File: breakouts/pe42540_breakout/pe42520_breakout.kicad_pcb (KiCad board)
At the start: 4 copper layers, 31.2 x 23.5 mm, 19 parts, among them P101 CONN_01X04, U101 CONN_SMA_2GND, U102 CONN_SMA_2GND, U103 CONN_SMA_2GND, U104 PE42540, U105 CONN_SMA_2GND, U106 CONN_SMA_2GND

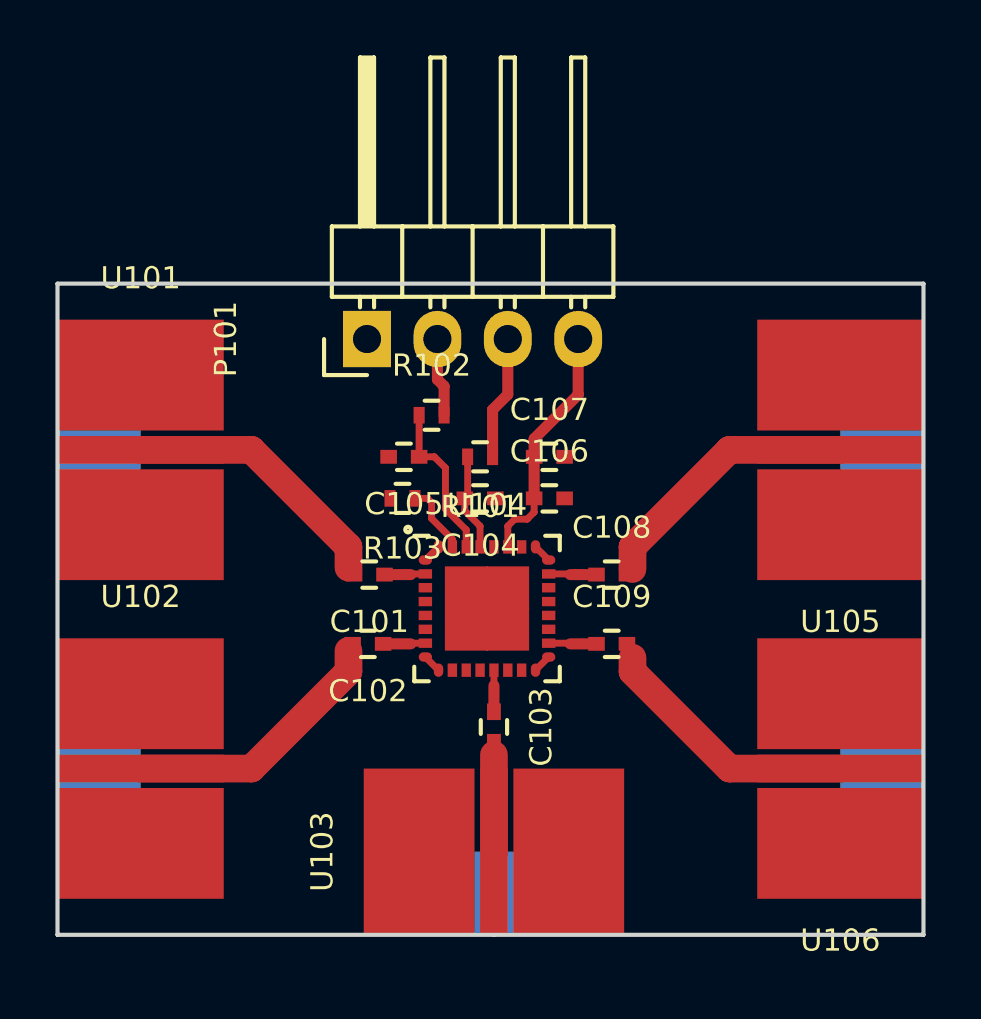
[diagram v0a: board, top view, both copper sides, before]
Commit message: ordered pe42540 breakout
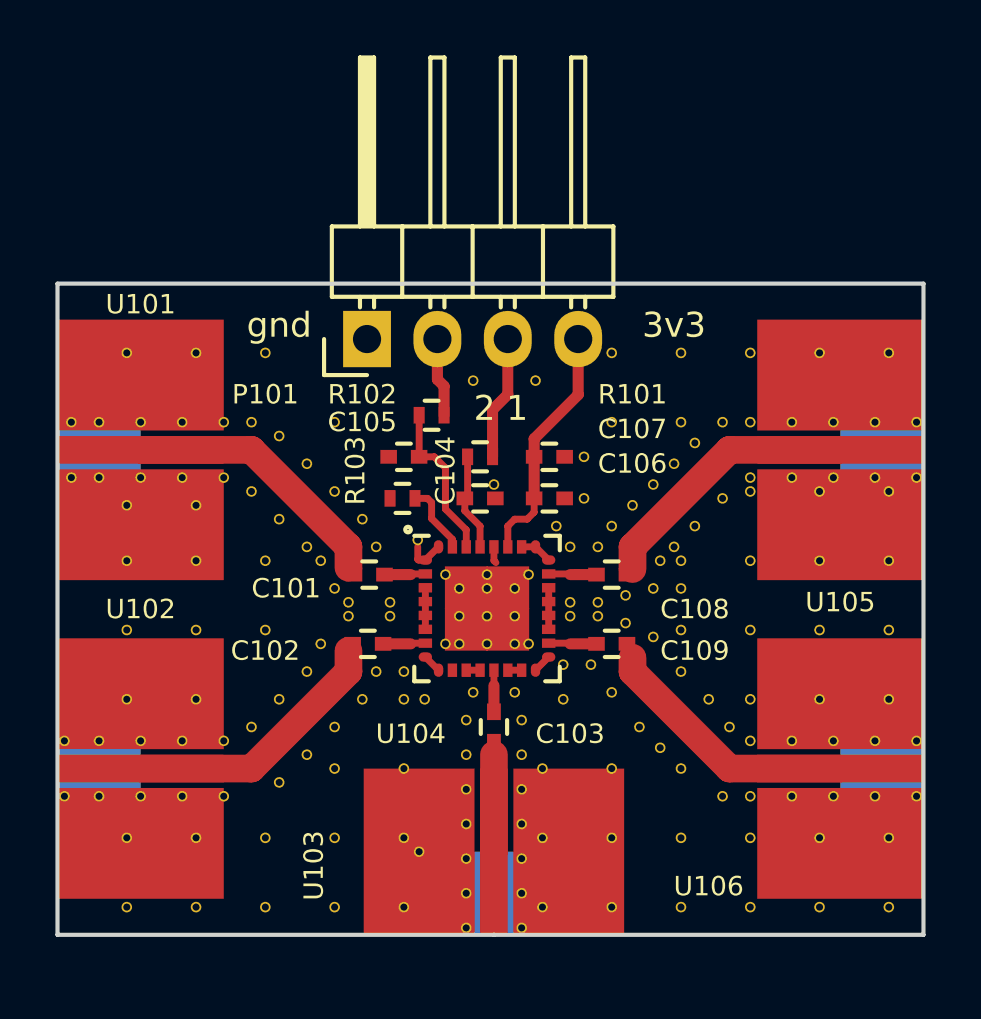
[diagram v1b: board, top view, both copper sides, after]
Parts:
- added REF**: VIA_OSH4LAYER_MIN, vna_footprints:VIA_OSH4LAYER_MIN, F.Cu at (162.5, 86.0)
- added REF**: VIA_OSH4LAYER_MIN, vna_footprints:VIA_OSH4LAYER_MIN, F.Cu at (160.0, 77.5)
- added REF**: VIA_OSH4LAYER_MIN, vna_footprints:VIA_OSH4LAYER_MIN, F.Cu at (154.8, 97.0)
- added REF**: VIA_OSH4LAYER_MIN, vna_footprints:VIA_OSH4LAYER_MIN, F.Cu at (154.8, 98.2)
- added REF**: VIA_OSH4LAYER_MIN, vna_footprints:VIA_OSH4LAYER_MIN, F.Cu at (156.8, 98.2)
- added REF**: VIA_OSH4LAYER_MIN, vna_footprints:VIA_OSH4LAYER_MIN, F.Cu at (152.0, 86.5)
- added REF**: VIA_OSH4LAYER_MIN, vna_footprints:VIA_OSH4LAYER_MIN, F.Cu at (150.5, 86.5)
- added REF**: VIA_OSH4LAYER_MIN, vna_footprints:VIA_OSH4LAYER_MIN, F.Cu at (161.0, 91.0)
- added REF**: VIA_OSH4LAYER_MIN, vna_footprints:VIA_OSH4LAYER_MIN, F.Cu at (162.5, 89.0)
- added REF**: VIA_OSH4LAYER_MIN, vna_footprints:VIA_OSH4LAYER_MIN, F.Cu at (164.0, 80.0)
- added REF**: VIA_OSH4LAYER_MIN, vna_footprints:VIA_OSH4LAYER_MIN, F.Cu at (163.0, 80.8)
- added REF**: VIA_OSH4LAYER_MIN, vna_footprints:VIA_OSH4LAYER_MIN, F.Cu at (161.5, 82.2)
- added REF**: VIA_OSH4LAYER_MIN, vna_footprints:VIA_OSH4LAYER_MIN, F.Cu at (160.0, 80.0)
- added REF**: VIA_OSH4LAYER_MIN, vna_footprints:VIA_OSH4LAYER_MIN, F.Cu at (162.2, 84.5)
- added REF**: VIA_OSH4LAYER_MIN, vna_footprints:VIA_OSH4LAYER_MIN, F.Cu at (160.8, 83.0)
- added REF**: VIA_OSH4LAYER_MIN, vna_footprints:VIA_OSH4LAYER_MIN, F.Cu at (161.5, 86.0)
- added REF**: VIA_OSH4LAYER_MIN, vna_footprints:VIA_OSH4LAYER_MIN, F.Cu at (160.5, 86.2)
- added REF**: VIA_OSH4LAYER_MIN, vna_footprints:VIA_OSH4LAYER_MIN, F.Cu at (158.5, 86.5)
- added REF**: VIA_OSH4LAYER_MIN, vna_footprints:VIA_OSH4LAYER_MIN, F.Cu at (158.5, 87.0)
- added REF**: VIA_OSH4LAYER_MIN, vna_footprints:VIA_OSH4LAYER_MIN, F.Cu at (159.5, 87.0)
- added REF**: VIA_OSH4LAYER_MIN, vna_footprints:VIA_OSH4LAYER_MIN, F.Cu at (159.5, 86.5)
- added REF**: VIA_OSH4LAYER_MIN, vna_footprints:VIA_OSH4LAYER_MIN, F.Cu at (159.5, 84.5)
- added REF**: VIA_OSH4LAYER_MIN, vna_footprints:VIA_OSH4LAYER_MIN, F.Cu at (158.5, 84.5)
- added REF**: VIA_OSH4LAYER_MIN, vna_footprints:VIA_OSH4LAYER_MIN, F.Cu at (162.5, 80.0)
- added REF**: VIA_OSH4LAYER_MIN, vna_footprints:VIA_OSH4LAYER_MIN, F.Cu at (154.5, 88.0)
- added REF**: VIA_OSH4LAYER_MIN, vna_footprints:VIA_OSH4LAYER_MIN, F.Cu at (154.5, 87.0)
- added REF**: VIA_OSH4LAYER_MIN, vna_footprints:VIA_OSH4LAYER_MIN, F.Cu at (154.5, 86.0)
- added REF**: VIA_OSH4LAYER_MIN, vna_footprints:VIA_OSH4LAYER_MIN, F.Cu at (155.5, 86.0)
- added REF**: VIA_OSH4LAYER_MIN, vna_footprints:VIA_OSH4LAYER_MIN, F.Cu at (155.5, 87.0)
- added REF**: VIA_OSH4LAYER_MIN, vna_footprints:VIA_OSH4LAYER_MIN, F.Cu at (156.5, 86.0)
- added REF**: VIA_OSH4LAYER_MIN, vna_footprints:VIA_OSH4LAYER_MIN, F.Cu at (156.5, 87.0)
- added REF**: VIA_OSH4LAYER_MIN, vna_footprints:VIA_OSH4LAYER_MIN, F.Cu at (156.5, 88.0)
- added REF**: VIA_OSH4LAYER_MIN, vna_footprints:VIA_OSH4LAYER_MIN, F.Cu at (155.5, 88.0)
- added REF**: VIA_OSH4LAYER_MIN, vna_footprints:VIA_OSH4LAYER_MIN, F.Cu at (155.5, 85.5)
- added REF**: VIA_OSH4LAYER_MIN, vna_footprints:VIA_OSH4LAYER_MIN, F.Cu at (162.5, 77.5)
- added REF**: VIA_OSH4LAYER_MIN, vna_footprints:VIA_OSH4LAYER_MIN, F.Cu at (165.0, 80.0)
- added REF**: VIA_OSH4LAYER_MIN, vna_footprints:VIA_OSH4LAYER_MIN, F.Cu at (166.5, 80.0)
- added REF**: VIA_OSH4LAYER_MIN, vna_footprints:VIA_OSH4LAYER_MIN, F.Cu at (168.0, 80.0)
- added REF**: VIA_OSH4LAYER_MIN, vna_footprints:VIA_OSH4LAYER_MIN, F.Cu at (169.5, 80.0)
- added REF**: VIA_OSH4LAYER_MIN, vna_footprints:VIA_OSH4LAYER_MIN, F.Cu at (171.0, 80.0)
- added REF**: VIA_OSH4LAYER_MIN, vna_footprints:VIA_OSH4LAYER_MIN, F.Cu at (164.0, 82.8)
- added REF**: VIA_OSH4LAYER_MIN, vna_footprints:VIA_OSH4LAYER_MIN, F.Cu at (165.0, 82.0)
- added REF**: VIA_OSH4LAYER_MIN, vna_footprints:VIA_OSH4LAYER_MIN, F.Cu at (166.5, 82.0)
- added REF**: VIA_OSH4LAYER_MIN, vna_footprints:VIA_OSH4LAYER_MIN, F.Cu at (168.0, 82.0)
- added REF**: VIA_OSH4LAYER_MIN, vna_footprints:VIA_OSH4LAYER_MIN, F.Cu at (169.5, 82.0)
- added REF**: VIA_OSH4LAYER_MIN, vna_footprints:VIA_OSH4LAYER_MIN, F.Cu at (165.0, 77.5)
- added REF**: VIA_OSH4LAYER_MIN, vna_footprints:VIA_OSH4LAYER_MIN, F.Cu at (171.0, 82.0)
- added REF**: VIA_OSH4LAYER_MIN, vna_footprints:VIA_OSH4LAYER_MIN, F.Cu at (163.5, 90.0)
- added REF**: VIA_OSH4LAYER_MIN, vna_footprints:VIA_OSH4LAYER_MIN, F.Cu at (162.5, 92.5)
- added REF**: VIA_OSH4LAYER_MIN, vna_footprints:VIA_OSH4LAYER_MIN, F.Cu at (164.0, 93.5)
- added REF**: VIA_OSH4LAYER_MIN, vna_footprints:VIA_OSH4LAYER_MIN, F.Cu at (165.0, 91.5)
- added REF**: VIA_OSH4LAYER_MIN, vna_footprints:VIA_OSH4LAYER_MIN, F.Cu at (165.0, 93.5)
- added REF**: VIA_OSH4LAYER_MIN, vna_footprints:VIA_OSH4LAYER_MIN, F.Cu at (166.5, 93.5)
- added REF**: VIA_OSH4LAYER_MIN, vna_footprints:VIA_OSH4LAYER_MIN, F.Cu at (166.5, 91.5)
- added REF**: VIA_OSH4LAYER_MIN, vna_footprints:VIA_OSH4LAYER_MIN, F.Cu at (168.0, 91.5)
- added REF**: VIA_OSH4LAYER_MIN, vna_footprints:VIA_OSH4LAYER_MIN, F.Cu at (168.0, 93.5)
- added REF**: VIA_OSH4LAYER_MIN, vna_footprints:VIA_OSH4LAYER_MIN, F.Cu at (167.5, 77.5)
- added REF**: VIA_OSH4LAYER_MIN, vna_footprints:VIA_OSH4LAYER_MIN, F.Cu at (169.5, 93.5)
- added REF**: VIA_OSH4LAYER_MIN, vna_footprints:VIA_OSH4LAYER_MIN, F.Cu at (169.5, 91.5)
- added REF**: VIA_OSH4LAYER_MIN, vna_footprints:VIA_OSH4LAYER_MIN, F.Cu at (171.0, 91.5)
- added REF**: VIA_OSH4LAYER_MIN, vna_footprints:VIA_OSH4LAYER_MIN, F.Cu at (171.0, 93.5)
- added REF**: VIA_OSH4LAYER_MIN, vna_footprints:VIA_OSH4LAYER_MIN, F.Cu at (152.5, 89.0)
- added REF**: VIA_OSH4LAYER_MIN, vna_footprints:VIA_OSH4LAYER_MIN, F.Cu at (150.0, 86.0)
- added REF**: VIA_OSH4LAYER_MIN, vna_footprints:VIA_OSH4LAYER_MIN, F.Cu at (151.0, 83.5)
- added REF**: VIA_OSH4LAYER_MIN, vna_footprints:VIA_OSH4LAYER_MIN, F.Cu at (150.0, 82.5)
- added REF**: VIA_OSH4LAYER_MIN, vna_footprints:VIA_OSH4LAYER_MIN, F.Cu at (149.0, 84.5)
- added REF**: VIA_OSH4LAYER_MIN, vna_footprints:VIA_OSH4LAYER_MIN, F.Cu at (149.0, 81.5)
- added REF**: VIA_OSH4LAYER_MIN, vna_footprints:VIA_OSH4LAYER_MIN, F.Cu at (170.0, 77.5)
- added REF**: VIA_OSH4LAYER_MIN, vna_footprints:VIA_OSH4LAYER_MIN, F.Cu at (148.0, 80.5)
- added REF**: VIA_OSH4LAYER_MIN, vna_footprints:VIA_OSH4LAYER_MIN, F.Cu at (148.0, 83.5)
- added REF**: VIA_OSH4LAYER_MIN, vna_footprints:VIA_OSH4LAYER_MIN, F.Cu at (147.0, 82.5)
- added REF**: VIA_OSH4LAYER_MIN, vna_footprints:VIA_OSH4LAYER_MIN, F.Cu at (147.0, 80.0)
- added REF**: VIA_OSH4LAYER_MIN, vna_footprints:VIA_OSH4LAYER_MIN, F.Cu at (146.0, 80.0)
- added REF**: VIA_OSH4LAYER_MIN, vna_footprints:VIA_OSH4LAYER_MIN, F.Cu at (146.0, 82.0)
- added REF**: VIA_OSH4LAYER_MIN, vna_footprints:VIA_OSH4LAYER_MIN, F.Cu at (144.5, 82.0)
- added REF**: VIA_OSH4LAYER_MIN, vna_footprints:VIA_OSH4LAYER_MIN, F.Cu at (144.5, 80.0)
- added REF**: VIA_OSH4LAYER_MIN, vna_footprints:VIA_OSH4LAYER_MIN, F.Cu at (143.0, 80.0)
- added REF**: VIA_OSH4LAYER_MIN, vna_footprints:VIA_OSH4LAYER_MIN, F.Cu at (143.0, 82.0)
- added REF**: VIA_OSH4LAYER_MIN, vna_footprints:VIA_OSH4LAYER_MIN, F.Cu at (165.0, 82.5)
- added REF**: VIA_OSH4LAYER_MIN, vna_footprints:VIA_OSH4LAYER_MIN, F.Cu at (141.5, 82.0)
- added REF**: VIA_OSH4LAYER_MIN, vna_footprints:VIA_OSH4LAYER_MIN, F.Cu at (141.5, 80.0)
- added REF**: VIA_OSH4LAYER_MIN, vna_footprints:VIA_OSH4LAYER_MIN, F.Cu at (140.5, 80.0)
- added REF**: VIA_OSH4LAYER_MIN, vna_footprints:VIA_OSH4LAYER_MIN, F.Cu at (140.5, 82.0)
- added REF**: VIA_OSH4LAYER_MIN, vna_footprints:VIA_OSH4LAYER_MIN, F.Cu at (149.5, 85.0)
- added REF**: VIA_OSH4LAYER_MIN, vna_footprints:VIA_OSH4LAYER_MIN, F.Cu at (151.5, 84.5)
- added REF**: VIA_OSH4LAYER_MIN, vna_footprints:VIA_OSH4LAYER_MIN, F.Cu at (154.0, 88.0)
- added REF**: VIA_OSH4LAYER_MIN, vna_footprints:VIA_OSH4LAYER_MIN, F.Cu at (154.0, 85.5)
- added REF**: VIA_OSH4LAYER_MIN, vna_footprints:VIA_OSH4LAYER_MIN, F.Cu at (152.0, 87.0)
- added REF**: VIA_OSH4LAYER_MIN, vna_footprints:VIA_OSH4LAYER_MIN, F.Cu at (150.5, 87.0)
- added REF**: VIA_OSH4LAYER_MIN, vna_footprints:VIA_OSH4LAYER_MIN, F.Cu at (167.5, 82.5)
- added REF**: VIA_OSH4LAYER_MIN, vna_footprints:VIA_OSH4LAYER_MIN, F.Cu at (151.5, 89.0)
- added REF**: VIA_OSH4LAYER_MIN, vna_footprints:VIA_OSH4LAYER_MIN, F.Cu at (151.0, 90.0)
- added REF**: VIA_OSH4LAYER_MIN, vna_footprints:VIA_OSH4LAYER_MIN, F.Cu at (149.5, 88.0)
- added REF**: VIA_OSH4LAYER_MIN, vna_footprints:VIA_OSH4LAYER_MIN, F.Cu at (150.0, 91.0)
- added REF**: VIA_OSH4LAYER_MIN, vna_footprints:VIA_OSH4LAYER_MIN, F.Cu at (149.0, 89.0)
- added REF**: VIA_OSH4LAYER_MIN, vna_footprints:VIA_OSH4LAYER_MIN, F.Cu at (149.0, 92.0)
- added REF**: VIA_OSH4LAYER_MIN, vna_footprints:VIA_OSH4LAYER_MIN, F.Cu at (148.0, 90.0)
- added REF**: VIA_OSH4LAYER_MIN, vna_footprints:VIA_OSH4LAYER_MIN, F.Cu at (148.0, 93.0)
- added REF**: VIA_OSH4LAYER_MIN, vna_footprints:VIA_OSH4LAYER_MIN, F.Cu at (147.0, 91.0)
- added REF**: VIA_OSH4LAYER_MIN, vna_footprints:VIA_OSH4LAYER_MIN, F.Cu at (146.0, 93.5)
- added REF**: VIA_OSH4LAYER_MIN, vna_footprints:VIA_OSH4LAYER_MIN, F.Cu at (170.0, 82.5)
- added REF**: VIA_OSH4LAYER_MIN, vna_footprints:VIA_OSH4LAYER_MIN, F.Cu at (146.0, 91.5)
- added REF**: VIA_OSH4LAYER_MIN, vna_footprints:VIA_OSH4LAYER_MIN, F.Cu at (144.5, 93.5)
- added REF**: VIA_OSH4LAYER_MIN, vna_footprints:VIA_OSH4LAYER_MIN, F.Cu at (144.5, 91.5)
- added REF**: VIA_OSH4LAYER_MIN, vna_footprints:VIA_OSH4LAYER_MIN, F.Cu at (143.0, 93.5)
- added REF**: VIA_OSH4LAYER_MIN, vna_footprints:VIA_OSH4LAYER_MIN, F.Cu at (143.0, 91.5)
- added REF**: VIA_OSH4LAYER_MIN, vna_footprints:VIA_OSH4LAYER_MIN, F.Cu at (141.5, 93.5)
- added REF**: VIA_OSH4LAYER_MIN, vna_footprints:VIA_OSH4LAYER_MIN, F.Cu at (141.5, 91.5)
- added REF**: VIA_OSH4LAYER_MIN, vna_footprints:VIA_OSH4LAYER_MIN, F.Cu at (140.2, 93.5)
- added REF**: VIA_OSH4LAYER_MIN, vna_footprints:VIA_OSH4LAYER_MIN, F.Cu at (140.2, 91.5)
- added REF**: VIA_OSH4LAYER_MIN, vna_footprints:VIA_OSH4LAYER_MIN, F.Cu at (157.0, 88.0)
- added REF**: VIA_OSH4LAYER_MIN, vna_footprints:VIA_OSH4LAYER_MIN, F.Cu at (170.0, 85.0)
- added REF**: VIA_OSH4LAYER_MIN, vna_footprints:VIA_OSH4LAYER_MIN, F.Cu at (167.5, 85.0)
- added REF**: VIA_OSH4LAYER_MIN, vna_footprints:VIA_OSH4LAYER_MIN, F.Cu at (165.0, 85.0)
- added REF**: VIA_OSH4LAYER_MIN, vna_footprints:VIA_OSH4LAYER_MIN, F.Cu at (162.5, 85.0)
- added REF**: VIA_OSH4LAYER_MIN, vna_footprints:VIA_OSH4LAYER_MIN, F.Cu at (162.5, 87.5)
- added REF**: VIA_OSH4LAYER_MIN, vna_footprints:VIA_OSH4LAYER_MIN, F.Cu at (165.0, 87.5)
- added REF**: VIA_OSH4LAYER_MIN, vna_footprints:VIA_OSH4LAYER_MIN, F.Cu at (167.5, 87.5)
- added REF**: VIA_OSH4LAYER_MIN, vna_footprints:VIA_OSH4LAYER_MIN, F.Cu at (170.0, 87.5)
- added REF**: VIA_OSH4LAYER_MIN, vna_footprints:VIA_OSH4LAYER_MIN, F.Cu at (170.0, 90.0)
- added REF**: VIA_OSH4LAYER_MIN, vna_footprints:VIA_OSH4LAYER_MIN, F.Cu at (167.5, 90.0)
- added REF**: VIA_OSH4LAYER_MIN, vna_footprints:VIA_OSH4LAYER_MIN, F.Cu at (157.0, 85.5)
- added REF**: VIA_OSH4LAYER_MIN, vna_footprints:VIA_OSH4LAYER_MIN, F.Cu at (165.0, 90.0)
- added REF**: VIA_OSH4LAYER_MIN, vna_footprints:VIA_OSH4LAYER_MIN, F.Cu at (160.0, 92.5)
- added REF**: VIA_OSH4LAYER_MIN, vna_footprints:VIA_OSH4LAYER_MIN, F.Cu at (160.0, 95.0)
- added REF**: VIA_OSH4LAYER_MIN, vna_footprints:VIA_OSH4LAYER_MIN, F.Cu at (162.5, 95.0)
- added REF**: VIA_OSH4LAYER_MIN, vna_footprints:VIA_OSH4LAYER_MIN, F.Cu at (165.0, 95.0)
- added REF**: VIA_OSH4LAYER_MIN, vna_footprints:VIA_OSH4LAYER_MIN, F.Cu at (167.5, 95.0)
- added REF**: VIA_OSH4LAYER_MIN, vna_footprints:VIA_OSH4LAYER_MIN, F.Cu at (170.0, 95.0)
- added REF**: VIA_OSH4LAYER_MIN, vna_footprints:VIA_OSH4LAYER_MIN, F.Cu at (170.0, 97.5)
- added REF**: VIA_OSH4LAYER_MIN, vna_footprints:VIA_OSH4LAYER_MIN, F.Cu at (167.5, 97.5)
- added REF**: VIA_OSH4LAYER_MIN, vna_footprints:VIA_OSH4LAYER_MIN, F.Cu at (165.0, 97.5)
- added REF**: VIA_OSH4LAYER_MIN, vna_footprints:VIA_OSH4LAYER_MIN, F.Cu at (142.5, 83.0)
- added REF**: VIA_OSH4LAYER_MIN, vna_footprints:VIA_OSH4LAYER_MIN, F.Cu at (162.5, 97.5)
- added REF**: VIA_OSH4LAYER_MIN, vna_footprints:VIA_OSH4LAYER_MIN, F.Cu at (160.0, 97.5)
- added REF**: VIA_OSH4LAYER_MIN, vna_footprints:VIA_OSH4LAYER_MIN, F.Cu at (152.5, 90.0)
- added REF**: VIA_OSH4LAYER_MIN, vna_footprints:VIA_OSH4LAYER_MIN, F.Cu at (150.0, 92.5)
- added REF**: VIA_OSH4LAYER_MIN, vna_footprints:VIA_OSH4LAYER_MIN, F.Cu at (152.5, 92.5)
- added REF**: VIA_OSH4LAYER_MIN, vna_footprints:VIA_OSH4LAYER_MIN, F.Cu at (153.1, 95.5)
- added REF**: VIA_OSH4LAYER_MIN, vna_footprints:VIA_OSH4LAYER_MIN, F.Cu at (152.5, 97.5)
- added REF**: VIA_OSH4LAYER_MIN, vna_footprints:VIA_OSH4LAYER_MIN, F.Cu at (142.5, 97.5)
- added REF**: VIA_OSH4LAYER_MIN, vna_footprints:VIA_OSH4LAYER_MIN, F.Cu at (145.0, 97.5)
- added REF**: VIA_OSH4LAYER_MIN, vna_footprints:VIA_OSH4LAYER_MIN, F.Cu at (147.5, 97.5)
- added REF**: VIA_OSH4LAYER_MIN, vna_footprints:VIA_OSH4LAYER_MIN, F.Cu at (145.0, 83.0)
- added REF**: VIA_OSH4LAYER_MIN, vna_footprints:VIA_OSH4LAYER_MIN, F.Cu at (150.0, 97.5)
- added REF**: VIA_OSH4LAYER_MIN, vna_footprints:VIA_OSH4LAYER_MIN, F.Cu at (150.0, 95.0)
- added REF**: VIA_OSH4LAYER_MIN, vna_footprints:VIA_OSH4LAYER_MIN, F.Cu at (147.5, 95.0)
- added REF**: VIA_OSH4LAYER_MIN, vna_footprints:VIA_OSH4LAYER_MIN, F.Cu at (145.0, 95.0)
- added REF**: VIA_OSH4LAYER_MIN, vna_footprints:VIA_OSH4LAYER_MIN, F.Cu at (142.5, 95.0)
- added REF**: VIA_OSH4LAYER_MIN, vna_footprints:VIA_OSH4LAYER_MIN, F.Cu at (150.0, 80.0)
- added REF**: VIA_OSH4LAYER_MIN, vna_footprints:VIA_OSH4LAYER_MIN, F.Cu at (147.5, 77.5)
- added REF**: VIA_OSH4LAYER_MIN, vna_footprints:VIA_OSH4LAYER_MIN, F.Cu at (145.0, 77.5)
- added REF**: VIA_OSH4LAYER_MIN, vna_footprints:VIA_OSH4LAYER_MIN, F.Cu at (142.5, 77.5)
- added REF**: VIA_OSH4LAYER_MIN, vna_footprints:VIA_OSH4LAYER_MIN, F.Cu at (142.5, 85.0)
- added REF**: VIA_OSH4LAYER_MIN, vna_footprints:VIA_OSH4LAYER_MIN, F.Cu at (152.5, 95.0)
- added REF**: VIA_OSH4LAYER_MIN, vna_footprints:VIA_OSH4LAYER_MIN, F.Cu at (145.0, 85.0)
- added REF**: VIA_OSH4LAYER_MIN, vna_footprints:VIA_OSH4LAYER_MIN, F.Cu at (147.5, 85.0)
- added REF**: VIA_OSH4LAYER_MIN, vna_footprints:VIA_OSH4LAYER_MIN, F.Cu at (147.5, 87.5)
- added REF**: VIA_OSH4LAYER_MIN, vna_footprints:VIA_OSH4LAYER_MIN, F.Cu at (145.0, 90.0)
- added REF**: VIA_OSH4LAYER_MIN, vna_footprints:VIA_OSH4LAYER_MIN, F.Cu at (145.0, 87.5)
- added REF**: VIA_OSH4LAYER_MIN, vna_footprints:VIA_OSH4LAYER_MIN, F.Cu at (142.5, 87.5)
- added REF**: VIA_OSH4LAYER_MIN, vna_footprints:VIA_OSH4LAYER_MIN, F.Cu at (142.5, 90.0)
- added REF**: VIA_OSH4LAYER_MIN, vna_footprints:VIA_OSH4LAYER_MIN, F.Cu at (153.0, 84.2)
- added REF**: VIA_OSH4LAYER_MIN, vna_footprints:VIA_OSH4LAYER_MIN, F.Cu at (158.2, 90.0)
- added REF**: VIA_OSH4LAYER_MIN, vna_footprints:VIA_OSH4LAYER_MIN, F.Cu at (162.2, 81.5)
- added REF**: VIA_OSH4LAYER_MIN, vna_footprints:VIA_OSH4LAYER_MIN, F.Cu at (157.5, 97.5)
- added REF**: VIA_OSH4LAYER_MIN, vna_footprints:VIA_OSH4LAYER_MIN, F.Cu at (161.8, 91.8)
- added REF**: VIA_OSH4LAYER_MIN, vna_footprints:VIA_OSH4LAYER_MIN, F.Cu at (153.2, 90.0)
- added REF**: VIA_OSH4LAYER_MIN, vna_footprints:VIA_OSH4LAYER_MIN, F.Cu at (158.0, 83.8)
- added REF**: VIA_OSH4LAYER_MIN, vna_footprints:VIA_OSH4LAYER_MIN, F.Cu at (159.0, 82.8)
- added REF**: VIA_OSH4LAYER_MIN, vna_footprints:VIA_OSH4LAYER_MIN, F.Cu at (159.0, 81.2)
- added REF**: VIA_OSH4LAYER_MIN, vna_footprints:VIA_OSH4LAYER_MIN, F.Cu at (157.2, 78.5)
- added REF**: VIA_OSH4LAYER_MIN, vna_footprints:VIA_OSH4LAYER_MIN, F.Cu at (155.0, 78.5)
- added REF**: VIA_OSH4LAYER_MIN, vna_footprints:VIA_OSH4LAYER_MIN, F.Cu at (155.8, 82.2)
- added REF**: VIA_OSH4LAYER_MIN, vna_footprints:VIA_OSH4LAYER_MIN, F.Cu at (164.2, 91.0)
- added REF**: VIA_OSH4LAYER_MIN, vna_footprints:VIA_OSH4LAYER_MIN, F.Cu at (163.0, 83.8)
- added REF**: VIA_OSH4LAYER_MIN, vna_footprints:VIA_OSH4LAYER_MIN, F.Cu at (157.5, 95.0)
- added REF**: VIA_OSH4LAYER_MIN, vna_footprints:VIA_OSH4LAYER_MIN, F.Cu at (161.8, 85.0)
- added REF**: VIA_OSH4LAYER_MIN, vna_footprints:VIA_OSH4LAYER_MIN, F.Cu at (160.0, 83.8)
- added REF**: VIA_OSH4LAYER_MIN, vna_footprints:VIA_OSH4LAYER_MIN, F.Cu at (160.5, 87.2)
- added REF**: VIA_OSH4LAYER_MIN, vna_footprints:VIA_OSH4LAYER_MIN, F.Cu at (161.5, 87.8)
- added REF**: VIA_OSH4LAYER_MIN, vna_footprints:VIA_OSH4LAYER_MIN, F.Cu at (160.0, 89.8)
- added REF**: VIA_OSH4LAYER_MIN, vna_footprints:VIA_OSH4LAYER_MIN, F.Cu at (159.2, 88.8)
- added REF**: VIA_OSH4LAYER_MIN, vna_footprints:VIA_OSH4LAYER_MIN, F.Cu at (158.2, 88.8)
- added REF**: VIA_OSH4LAYER_MIN, vna_footprints:VIA_OSH4LAYER_MIN, F.Cu at (156.5, 89.8)
- added REF**: VIA_OSH4LAYER_MIN, vna_footprints:VIA_OSH4LAYER_MIN, F.Cu at (155.0, 89.8)
- added REF**: VIA_OSH4LAYER_MIN, vna_footprints:VIA_OSH4LAYER_MIN, F.Cu at (154.8, 90.8)
- added REF**: VIA_OSH4LAYER_MIN, vna_footprints:VIA_OSH4LAYER_MIN, F.Cu at (157.5, 92.5)
- added REF**: VIA_OSH4LAYER_MIN, vna_footprints:VIA_OSH4LAYER_MIN, F.Cu at (156.8, 90.8)
- added REF**: VIA_OSH4LAYER_MIN, vna_footprints:VIA_OSH4LAYER_MIN, F.Cu at (156.8, 92.0)
- added REF**: VIA_OSH4LAYER_MIN, vna_footprints:VIA_OSH4LAYER_MIN, F.Cu at (154.8, 92.0)
- added REF**: VIA_OSH4LAYER_MIN, vna_footprints:VIA_OSH4LAYER_MIN, F.Cu at (154.8, 93.2)
- added REF**: VIA_OSH4LAYER_MIN, vna_footprints:VIA_OSH4LAYER_MIN, F.Cu at (156.8, 93.2)
- added REF**: VIA_OSH4LAYER_MIN, vna_footprints:VIA_OSH4LAYER_MIN, F.Cu at (156.8, 94.5)
- added REF**: VIA_OSH4LAYER_MIN, vna_footprints:VIA_OSH4LAYER_MIN, F.Cu at (154.8, 94.5)
- added REF**: VIA_OSH4LAYER_MIN, vna_footprints:VIA_OSH4LAYER_MIN, F.Cu at (154.8, 95.8)
- added REF**: VIA_OSH4LAYER_MIN, vna_footprints:VIA_OSH4LAYER_MIN, F.Cu at (156.8, 95.8)
- added REF**: VIA_OSH4LAYER_MIN, vna_footprints:VIA_OSH4LAYER_MIN, F.Cu at (156.8, 97.0)
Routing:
- net GND: track 2.69 -> 8.52 mm
- added copper zone on B.Cu, net GND
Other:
- net class Default: clearance 0.2 -> 0.126
- rule trace_clearance: 0.2 -> 0.126
- board text added: "2 1"
- board text added: "3v3"
- board text added: "gnd"
- board text added: "pe42540 4-way switch breakout"
